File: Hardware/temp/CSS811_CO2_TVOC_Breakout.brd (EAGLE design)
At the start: 17.8 x 17.8 mm, 20 parts, among them U2 CCS811

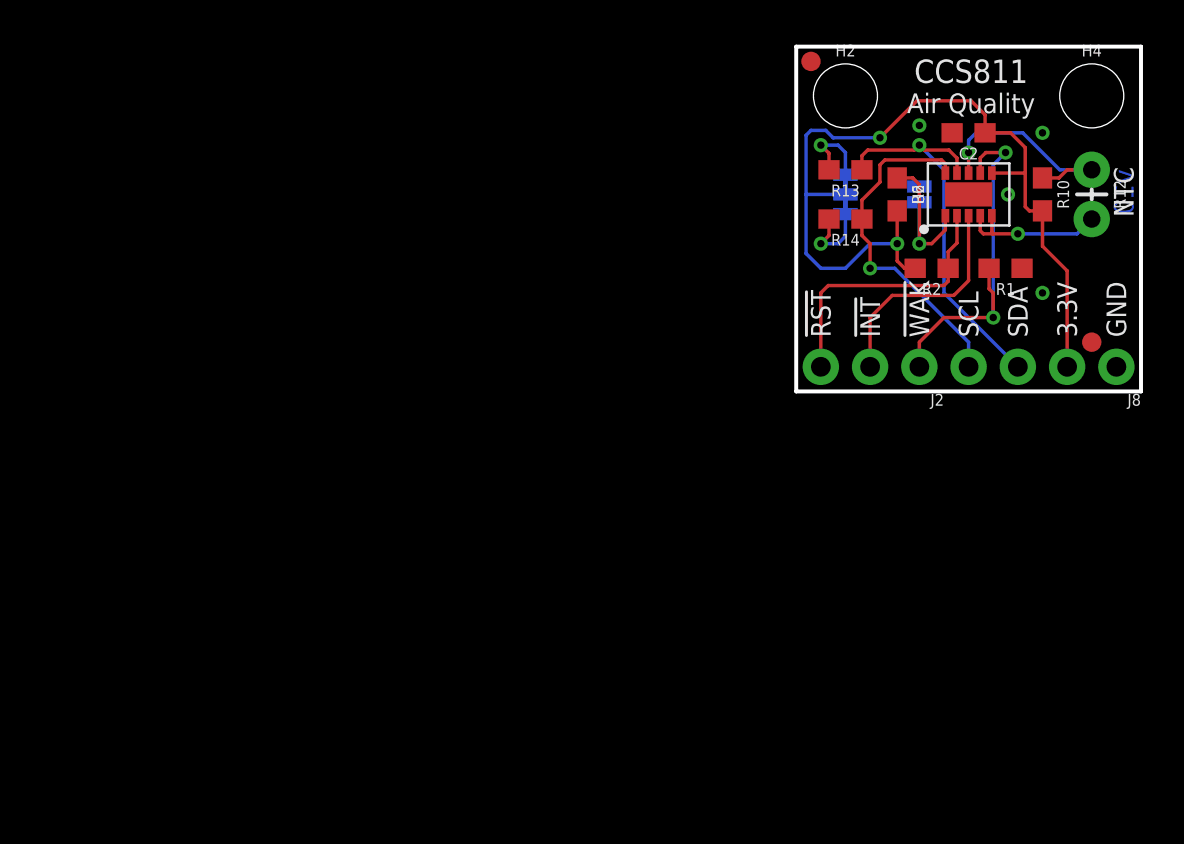
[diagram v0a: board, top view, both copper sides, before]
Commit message: Added temp library of new parts, added proper gitignore/gitattributes, switched sparkfun logo in for sparkx logo, cleaned up schematic, changed version number to v10
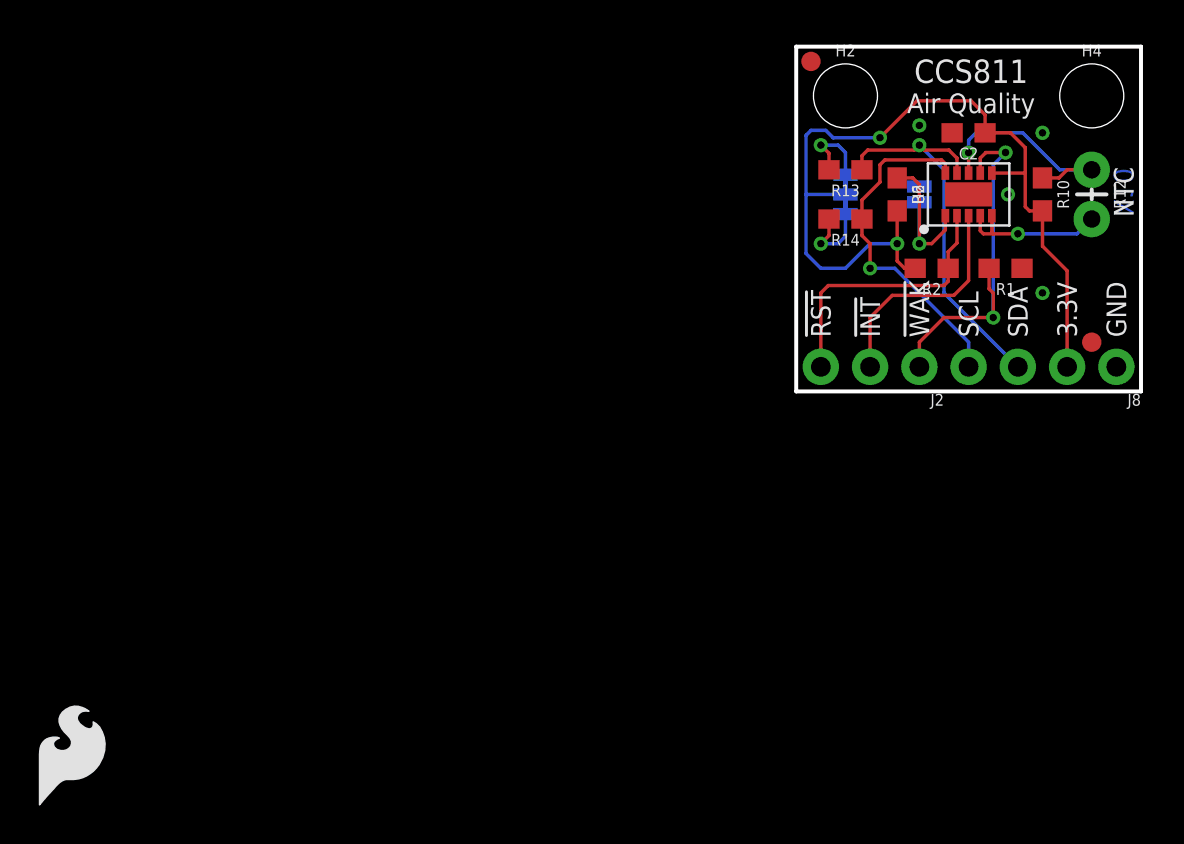
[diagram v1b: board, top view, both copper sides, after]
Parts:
- moved LOGO1 60.0 mm to (-39.4, -21.6), flipped to the top
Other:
- board text added: "X10"
- board text removed: "v10"
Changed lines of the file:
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@@
 <grid distance="0.05" unitdist="inch" unit="inch" style="lines" multiple="1" display="yes" altdistance="0.005" altunitdist="inch" altunit="inch"/>
 <layers>
-<layer number="1" name="Top" color="4" fill="1" visible="no" active="yes"/>
+<layer number="1" name="Top" color="4" fill="1" visible="yes" active="yes"/>
 <layer number="2" name="Route2" color="1" fill="3" visible="no" active="no"/>
 <layer number="3" name="Route3" color="4" fill="3" visible="no" active="no"/>
@@
 <layer number="19" name="Unrouted" color="6" fill="1" visible="yes" active="yes"/>
 <layer number="20" name="Dimension" color="15" fill="1" visible="yes" active="yes"/>
-<layer number="21" name="tPlace" color="16" fill="1" visible="no" active="yes"/>
+<layer number="21" name="tPlace" color="16" fill="1" visible="yes" active="yes"/>
 <layer number="22" name="bPlace" color="14" fill="1" visible="yes" active="yes"/>
-<layer number="23" name="tOrigins" color="15" fill="1" visible="no" active="yes"/>
+<layer number="23" name="tOrigins" color="15" fill="1" visible="yes" active="yes"/>
 <layer number="24" name="bOrigins" color="15" fill="1" visible="yes" active="yes"/>
 <layer number="25" name="tNames" color="7" fill="1" visible="no" active="yes"/>
@@
 <layer number="43" name="vRestrict" color="2" fill="10" visible="no" active="yes"/>
 <layer number="44" name="Drills" color="7" fill="1" visible="no" active="yes"/>
-<layer number="45" name="Holes" color="7" fill="1" visible="no" active="yes"/>
+<layer number="45" name="Holes" color="7" fill="1" visible="yes" active="yes"/>
 <layer number="46" name="Milling" color="3" fill="1" visible="no" active="yes"/>
 <layer number="47" name="Measures" color="7" fill="1" visible="no" active="yes"/>
@@
 <layer number="49" name="Reference" color="7" fill="1" visible="no" active="yes"/>
 <layer number="50" name="dxf" color="7" fill="1" visible="no" active="no"/>
-<layer number="51" name="tDocu" color="6" fill="1" visible="no" active="yes"/>
+<layer number="51" name="tDocu" color="6" fill="1" visible="yes" active="yes"/>
 <layer number="52" name="bDocu" color="7" fill="1" visible="no" active="yes"/>
 <layer number="53" name="tGND_GNDA" color="7" fill="9" visible="no" active="no"/>
@@
 <text x="16.51" y="2.794" size="1.016" layer="22" font="vector" ratio="15" rot="MR90" align="center-left">GND</text>
 <text x="9.017" y="16.51" size="1.2065" layer="21" ratio="15" align="center">CCS811</text>
-<text x="17.399" y="10.287" size="1.016" layer="16" ratio="20" rot="SMR270" align="bottom-center">v10</text>
+<text x="17.399" y="10.287" size="1.016" layer="16" ratio="20" rot="MR270" align="bottom-center">X10</text>
 <text x="4.191" y="10.287" size="0.889" layer="22" ratio="15" rot="MR90" align="bottom-center">ADDR</text>
 <text x="16.51" y="-21.59" size="1.778" layer="51">Nathan Seidle</text>
@@
 <attribute name="PROD_ID" value="RES-07828" x="10.795" y="6.35" size="1.778" layer="27" font="vector" ratio="15" rot="R180" display="off"/>
 </element>
-<element name="LOGO1" library="SparkFun-Aesthetics" package="SFE_LOGO_FLAME_.2" value="SFE_LOGO_FLAME.2_INCH" x="10.922" y="11.049" rot="MR0"/>
+<element name="LOGO1" library="SparkFun-Aesthetics" package="SFE_LOGO_FLAME_.2" value="SFE_LOGO_FLAME.2_INCH" x="-39.37" y="-21.59"/>
 </elements>
 <signals>
